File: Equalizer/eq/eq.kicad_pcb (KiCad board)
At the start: 2 copper layers, 59 x 56.5 mm, 48 parts, among them J1 Conn_01x04_Pin, U1 TL074, U2 TL074

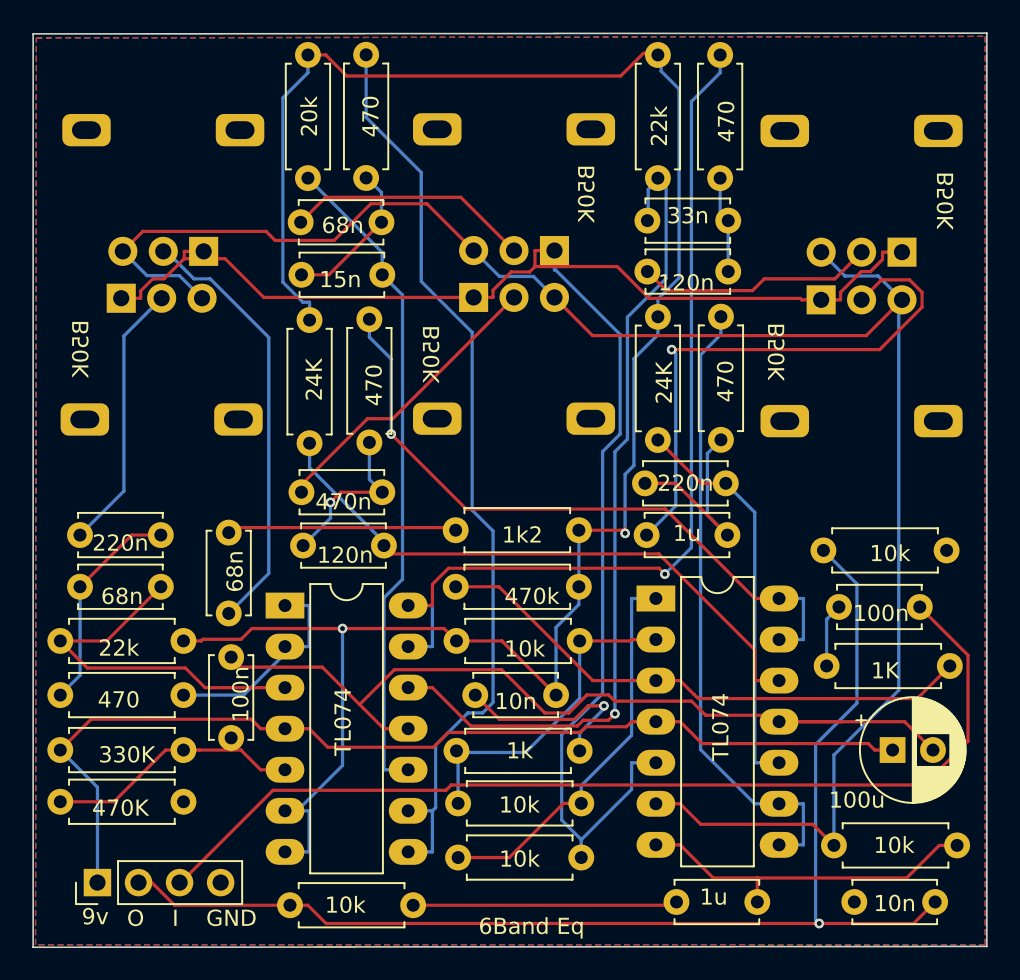
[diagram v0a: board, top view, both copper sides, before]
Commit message: added engineers thumb, ramshead-bmp
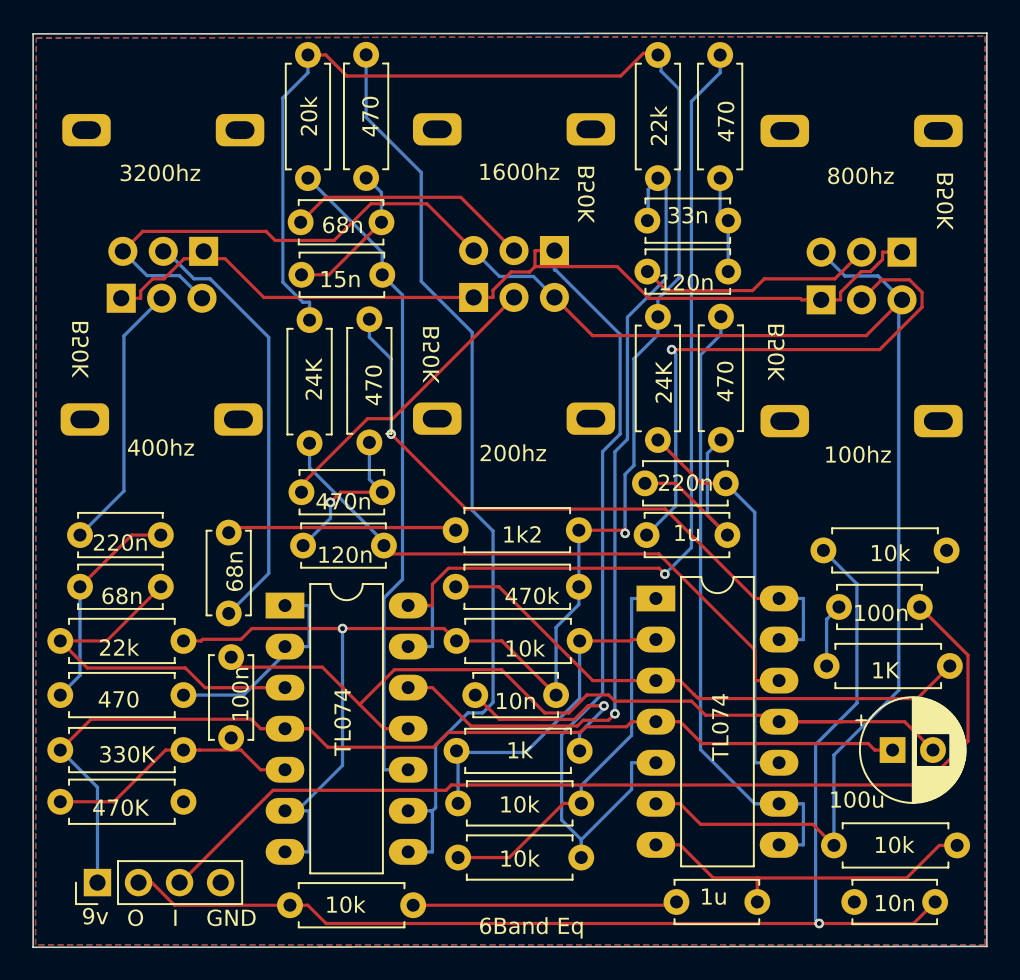
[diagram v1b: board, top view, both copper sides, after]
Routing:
- net Net-(U1B-+): track 106.9 -> 105.3 mm
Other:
- board text added: "100hz"
- board text added: "1600hz"
- board text added: "200hz"
- board text added: "3200hz"
- board text added: "400hz"
- board text added: "800hz"
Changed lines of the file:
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@@
   (gr_line (start 159 156.45) (end 159 99.95)
     (stroke (width 0.1) (type solid)) (layer "Edge.Cuts"))
+  (gr_text "100hz" (at 148.91 126.64) (layer "F.SilkS")
+    (effects (font (size 1 1) (thickness 0.1)) (justify left bottom))
+  )
   (gr_text "6Band Eq	\n" (at 127.55 155.8) (layer "F.SilkS")
     (effects (font (size 1 1) (thickness 0.1)) (justify left bottom))
   )
+  (gr_text "3200hz\n" (at 105.31 109.22) (layer "F.SilkS")
+    (effects (font (size 1 1) (thickness 0.1)) (justify left bottom))
+  )
   (gr_text "9v" (at 103 155.2) (layer "F.SilkS")
     (effects (font (size 1 1) (thickness 0.1)) (justify left bottom))
   )
+  (gr_text "400hz" (at 105.8 126.21) (layer "F.SilkS")
+    (effects (font (size 1 1) (thickness 0.1)) (justify left bottom))
+  )
+  (gr_text "800hz" (at 149.09 109.4) (layer "F.SilkS")
+    (effects (font (size 1 1) (thickness 0.1)) (justify left bottom))
+  )
   (gr_text "O" (at 105.8 155.3) (layer "F.SilkS")
     (effects (font (size 1 1) (thickness 0.1)) (justify left bottom))
@@
     (effects (font (size 1 1) (thickness 0.1)) (justify left bottom))
   )
+  (gr_text "1600hz\n" (at 127.52 109.15) (layer "F.SilkS")
+    (effects (font (size 1 1) (thickness 0.1)) (justify left bottom))
+  )
   (gr_text "GND\n" (at 110.7 155.3) (layer "F.SilkS")
+    (effects (font (size 1 1) (thickness 0.1)) (justify left bottom))
+  )
+  (gr_text "200hz" (at 127.58 126.55) (layer "F.SilkS")
     (effects (font (size 1 1) (thickness 0.1)) (justify left bottom))
   )
@@
   (segment (start 109.3481 113.9008) (end 108.1008 115.1481) (width 0.2) (layer "F.Cu") (net 33))
   (segment (start 151.2285 114.7019) (end 151.797 114.7019) (width 0.2) (layer "F.Cu") (net 33))
-  (segment (start 110.55 113.45) (end 109.3481 113.45) (width 0.2) (layer "F.Cu") (net 33))
   (segment (start 108.1008 115.1481) (end 107.403 115.1481) (width 0.2) (layer "F.Cu") (net 33))
   (segment (start 149.351 116.45) (end 149.9519 116.45) (width 0.2) (layer "F.Cu") (net 33))
@@
   (segment (start 131.0481 113.4) (end 131.0481 114.3909) (width 0.2) (layer "F.Cu") (net 33))
   (segment (start 148.75 116.45) (end 147.5481 116.45) (width 0.2) (layer "F.Cu") (net 33))
-  (segment (start 109.3481 113.45) (end 109.3481 113.9008) (width 0.2) (layer "F.Cu") (net 33))
   (segment (start 130.7146 114.7244) (end 129.5767 114.7244) (width 0.2) (layer "F.Cu") (net 33))
   (segment (start 138.1016 116.3599) (end 147.458 116.3599) (width 0.2) (layer "F.Cu") (net 33))
